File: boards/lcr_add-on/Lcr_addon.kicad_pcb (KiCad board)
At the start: 2 copper layers, 85.1 x 55.1 mm, 19 parts, among them J2 LCr_ conector, J4 blank in, J5 Green control output, J6 Blue control output, J7 Red control output, J8 blank_jumper, U1 SN74LS08N, U2 SN74LS08N, U3 SN74HC14N, U4 LM2596T-5

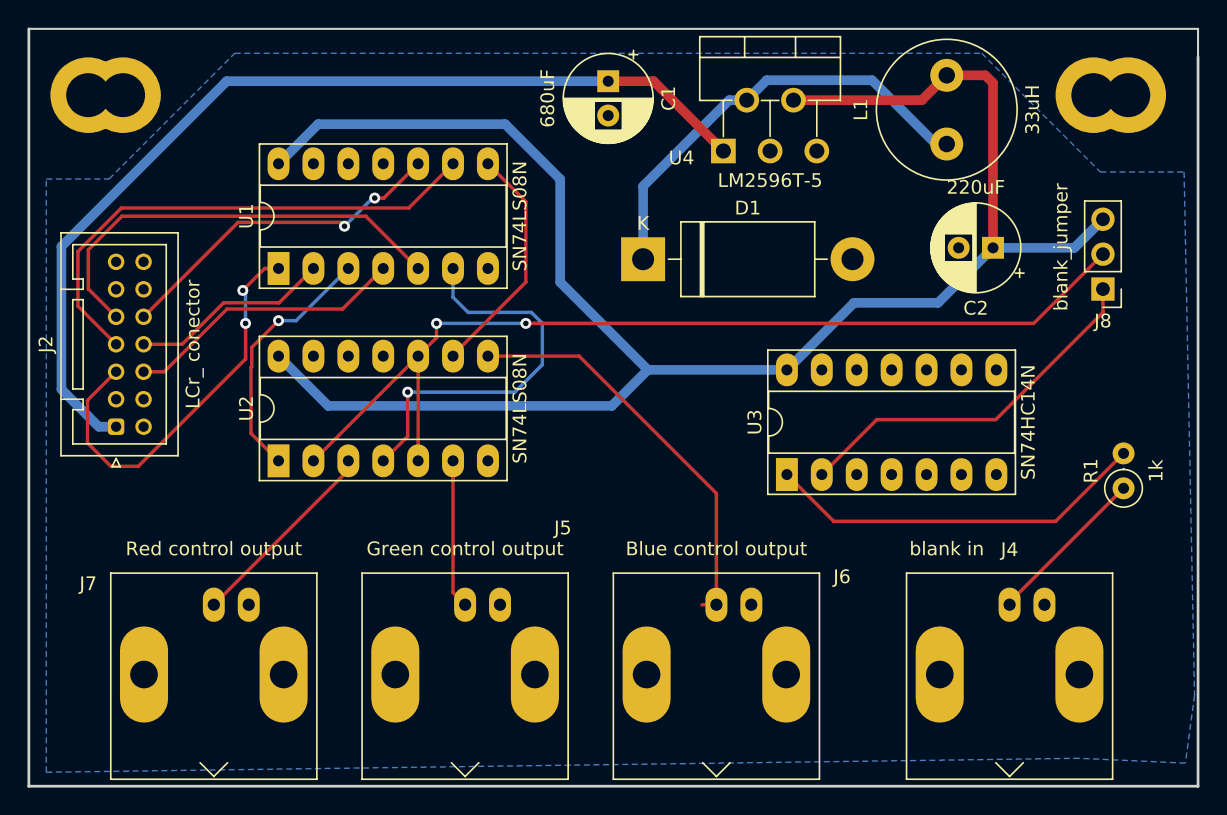
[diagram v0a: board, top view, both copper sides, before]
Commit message: update LCR-addon board
- solve mounting holes
- solve alignment target on the user layer
- check connections
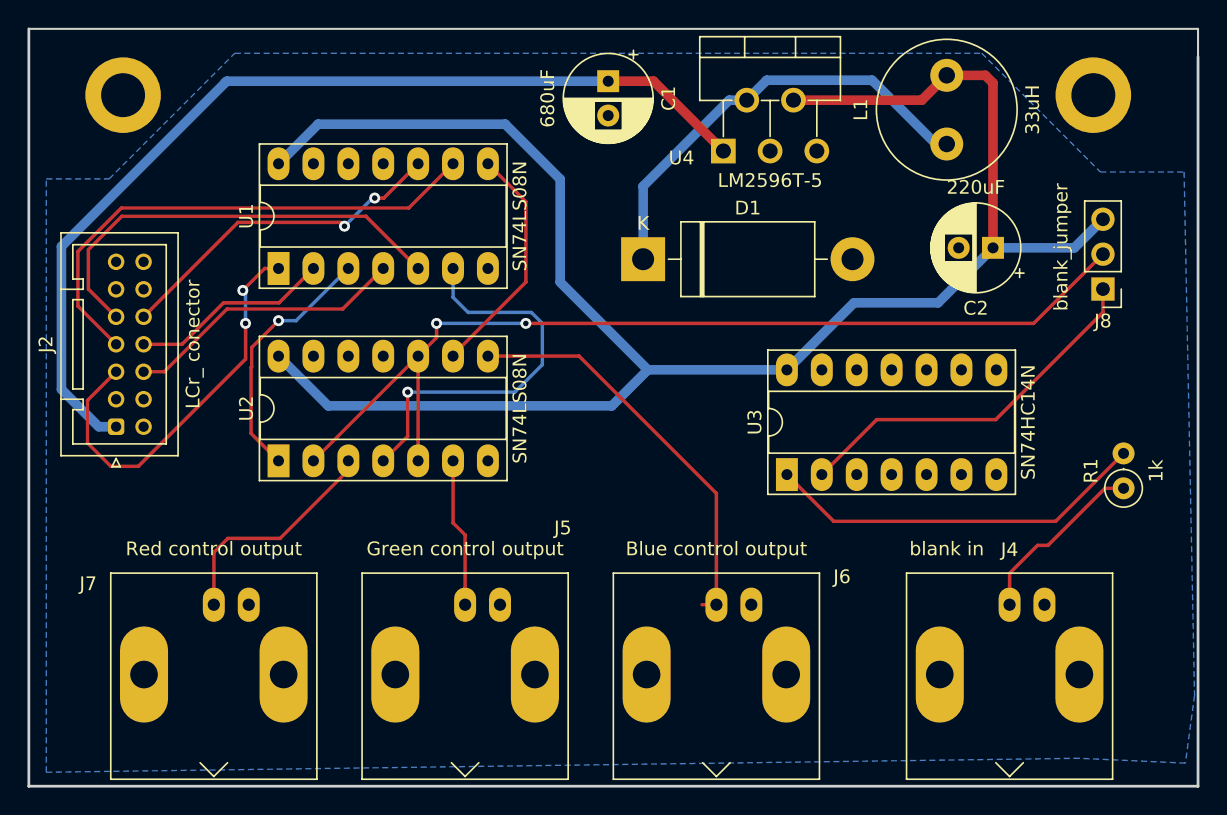
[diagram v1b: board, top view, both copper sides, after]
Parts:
- removed the REF** at (116.8, 56.4)
- removed the REF** at (41.1, 56.4)
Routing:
- net Net-(J7-Pad1): track 15.0 -> 17.2 mm
- net Net-(J4-Pad1): track 11.9 -> 13.3 mm
